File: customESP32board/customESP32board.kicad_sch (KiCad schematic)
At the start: 27 parts, among them J1 USB_B_Micro, J2 Conn_01x16_Pin, J3 Conn_01x16_Pin, Q1 S8050, Q2 S8050, SW1 SW_Push, SW2 SW_Push, U1 ESP32-WROOM-32, U2 CH340C, U3 AMS1117-3.3

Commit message: finalized esp32 board schematic
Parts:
- added D6, D7, D8: LED_BGKR, symbol Device:LED_BGKR
- added R7, R8, R9: 220 Ohm, symbol Device:R
- R1, R4: value 80 Ohm -> 1k Ohm
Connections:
- net ESP_RXD is gone; now on net ESP_U0TX: U2.3 (RXD)
- net ESP_TXD is gone; now on net ESP_U0RX: U2.2 (TXD)
- net ESP_IO0: now also U1.25 (IO0)
- net ESP_IO12: now also U1.14 (IO12)
- net ESP_IO13: now also U1.16 (IO13)
- net ESP_IO14: now also U1.13 (IO14)
- net ESP_IO15: now also U1.23 (IO15)
- net ESP_IO16: now also U1.27 (IO16)
- net ESP_IO17: now also U1.28 (IO17)
- net ESP_IO18: now also U1.30 (IO18), R9.1
- net ESP_IO19: now also U1.31 (IO19), R8.1
- net ESP_IO2: now also U1.24 (IO2)
- net ESP_IO21: now also U1.33 (IO21), R7.1
- net ESP_IO22: now also U1.36 (IO22)
- net ESP_IO23: now also U1.37 (IO23)
- net ESP_IO25: now also U1.10 (IO25)
- net ESP_IO26: now also U1.11 (IO26)
- net ESP_IO27: now also U1.12 (IO27)
- net ESP_IO32: now also U1.8 (IO32)
- net ESP_IO4: now also U1.26 (IO4)
- net ESP_IO5: now also U1.29 (IO5)
- net ESP_U0RX: now also U1.34 (RXD0/IO3)
- net ESP_U0TX: now also U1.35 (TXD0/IO1)
- net GND: now also D6.3 (K), D7.3 (K), D8.3 (K)
- new net RGB_BLUE: D6.1 (BA), D7.1 (BA), D8.1 (BA), R7.2
- new net RGB_GREEN: D6.2 (GA), D7.2 (GA), D8.2 (GA), R8.2
- new net RGB_RED: D6.4 (RA), D7.4 (RA), D8.4 (RA), R9.2
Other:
- note added: "3 RGBs common Cathode"
- note added: "BOOT"
- note added: "ESP32-Wroom-32"
- note added: "Reset"
- moved on the sheet: C1, C11, C3, C6, C7, D1, D2, D3, D4, D5, D9, J1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

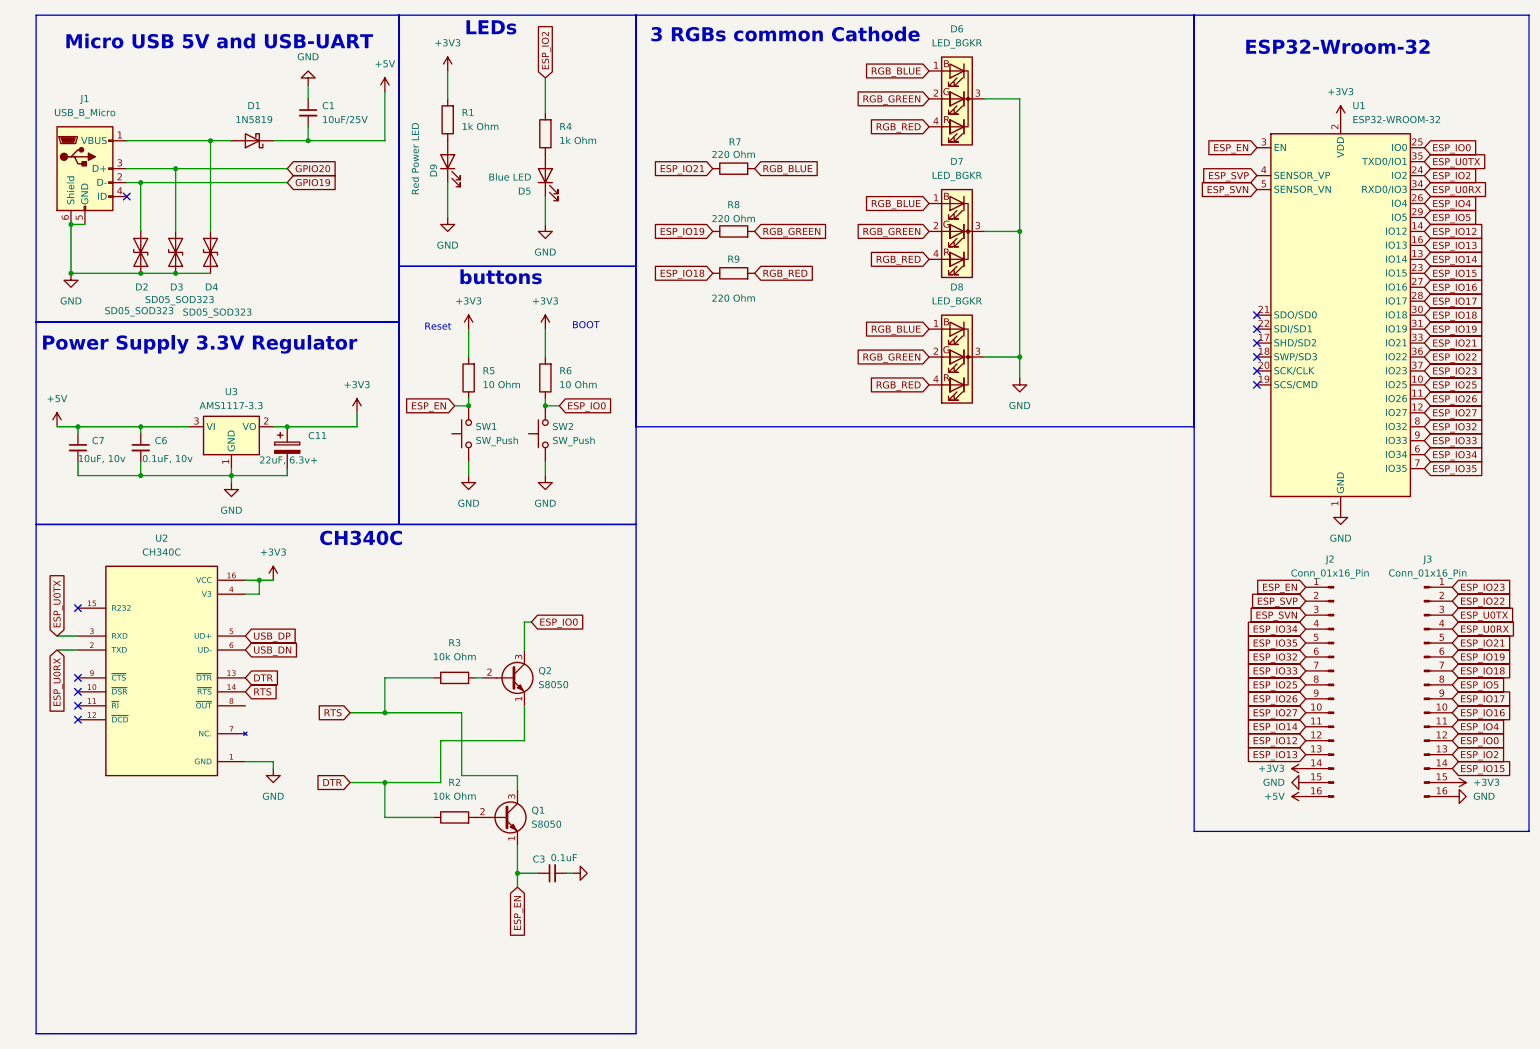
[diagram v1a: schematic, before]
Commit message: calculated LEDs current limiting resistance for power and test led D9 and D5
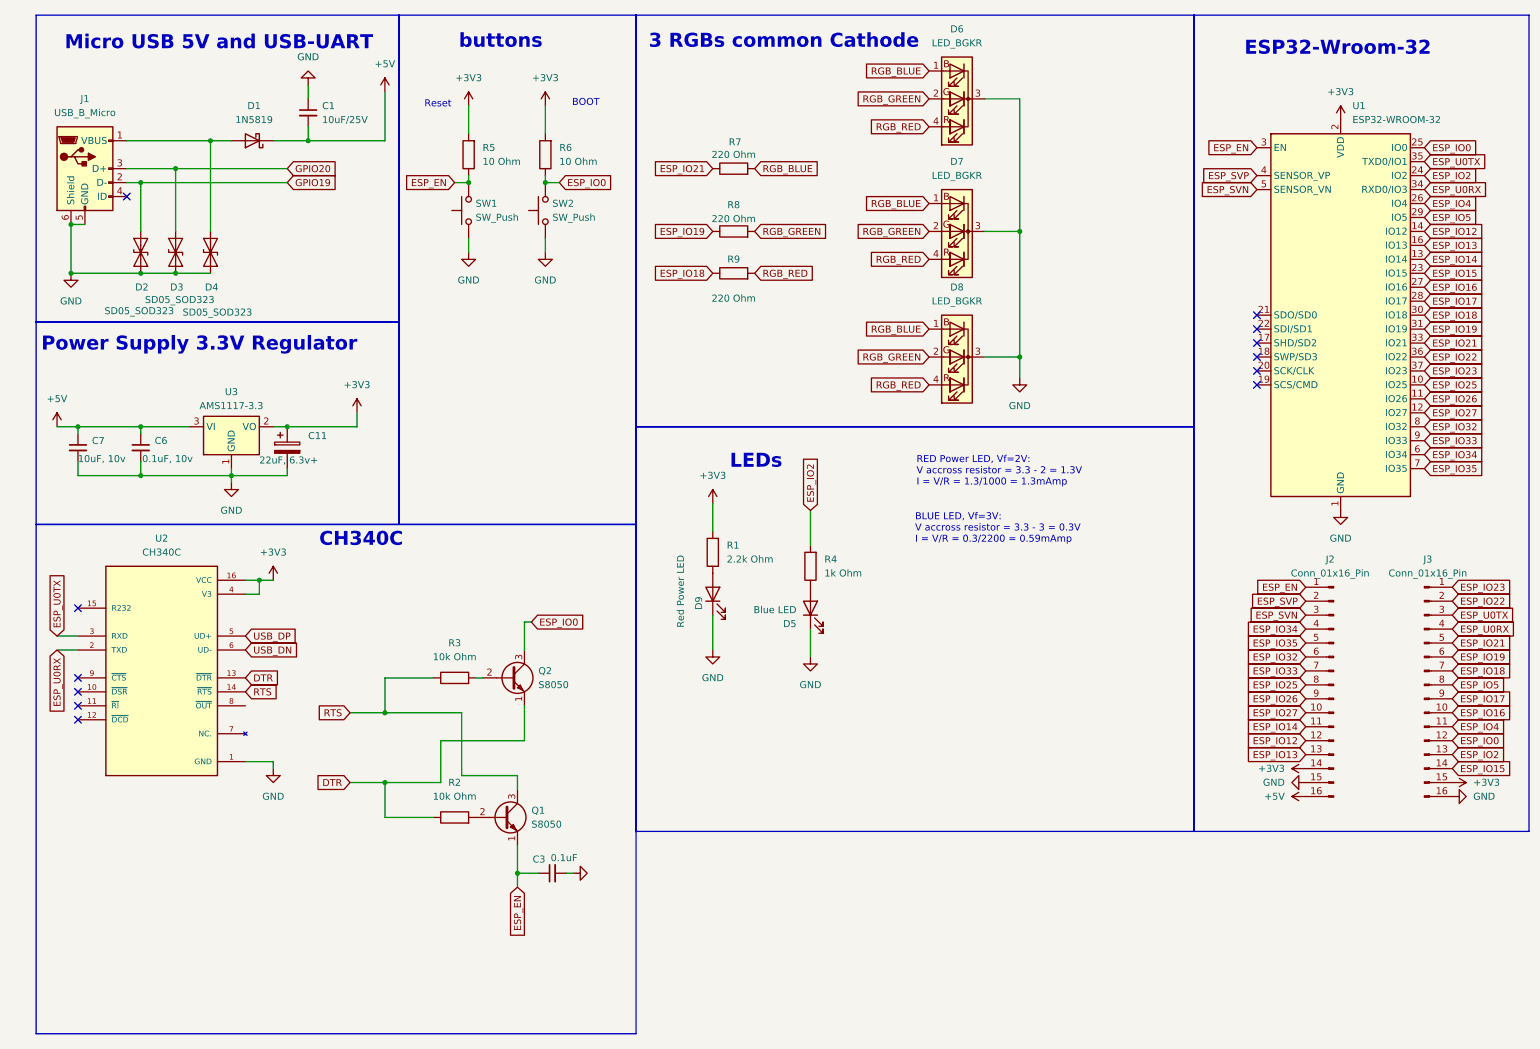
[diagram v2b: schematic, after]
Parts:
- R1: value 1k Ohm -> 2.2k Ohm
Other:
- note added: "BLUE LED, Vf=3V: V accross resistor = 3.3 - 3 = 0.3V I = V/R = 0.3/2200 = 0.59mAmp"
- note added: "RED Power LED, Vf=2V: V accross resistor = 3.3 - 2 = 1.3V I = V/R = 1.3/1000 = 1.3mAmp"
- moved on the sheet: D5, D9, R1, R4, R5, R6, SW1, SW2

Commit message: added RGB controlled by esp32 pins using N channel MOSFET bss138
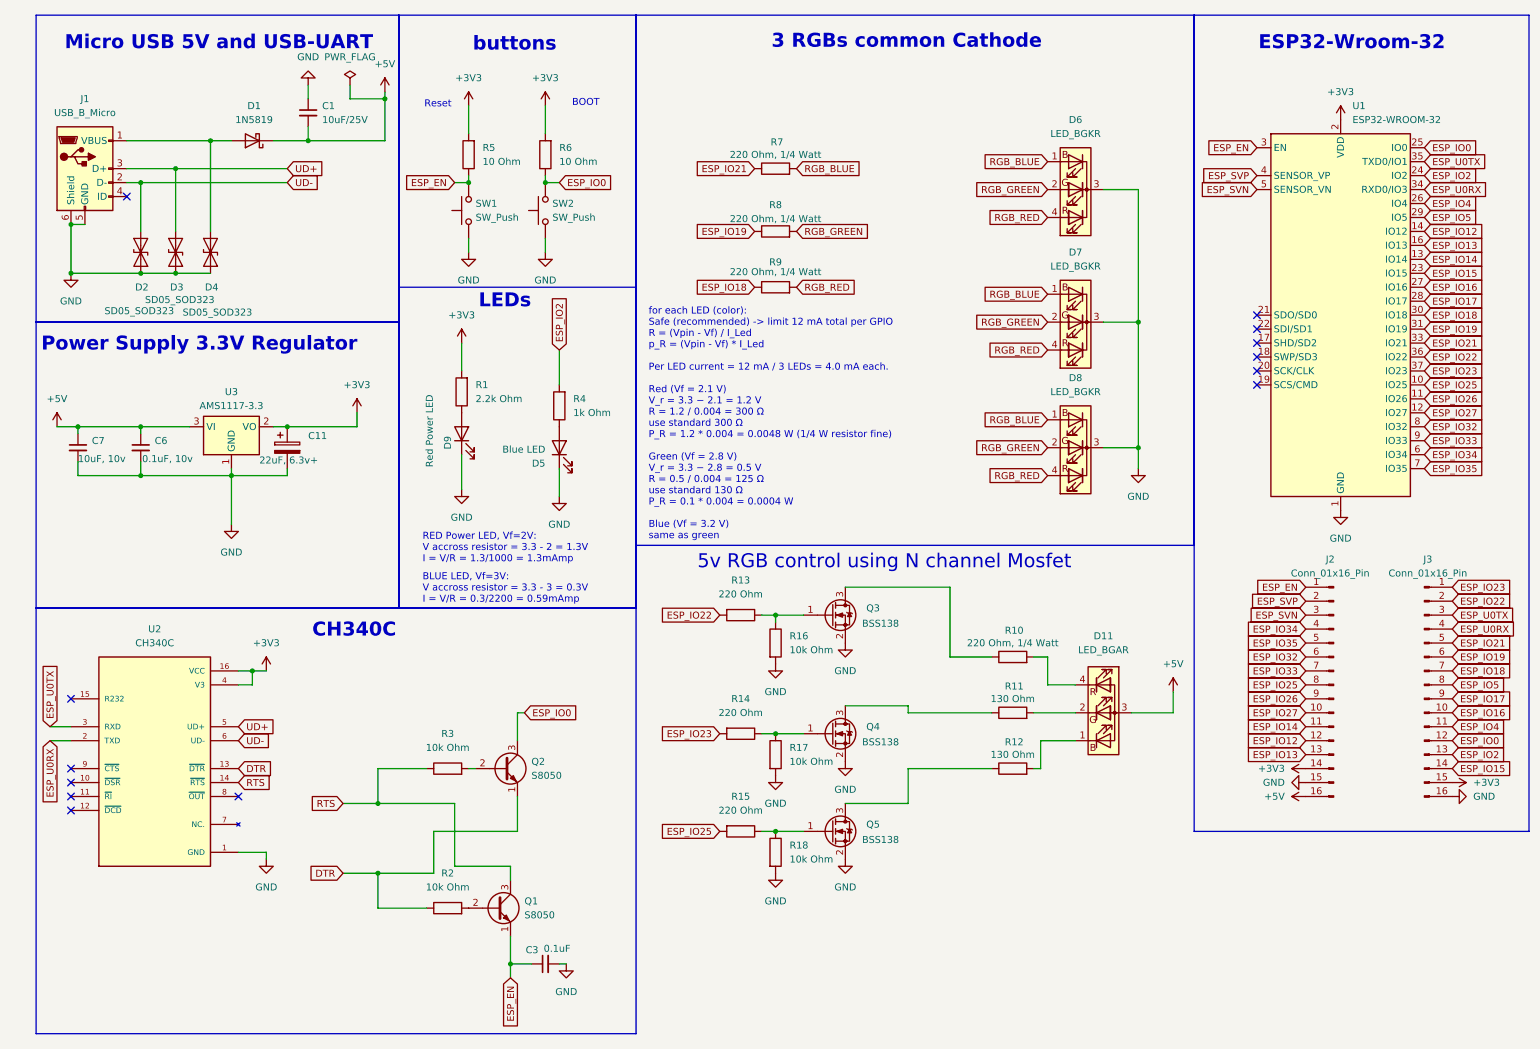
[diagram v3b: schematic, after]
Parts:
- added D11: LED_BGAR, symbol Device:LED_BGAR
- added Q3, Q4, Q5: BSS138, Package_TO_SOT_SMD:SOT-23, symbol Transistor_FET:BSS138
- added R10: 220 Ohm, 1/4 Watt, symbol Device:R
- added R11, R12: 130 Ohm, symbol Device:R
- added R13, R14, R15: 220 Ohm, symbol Device:R
- added R16, R17, R18: 10k Ohm, symbol Device:R
- D1: link (none) -> https://uge-one.com/product/smd-schottky-diode-1n5819-ss14-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
- D2, D3, D4: link (none) -> https://uge-one.com/product/smd-tvs-esd-protection-diode-bi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
- D5, D9: link (none) -> https://makerselectronics.com/product/smd-led-0603/?srsltid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
- D6, D7, D8: link (none) -> https://makerselectronics.com/product/rgb-diffused-led-comm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
- J1: link (none) -> https://uge-one.com/product/micro-usb-5pin-smd-connector-4-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
- Q1, Q2: link (none) -> https://makerselectronics.com/product/smd-transistor-s8050-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
- R1: link (none) -> https://makerselectronics.com/product/chip-resistor-smd-2-2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
- R2, R3: link (none) -> https://makerselectronics.com/product/chip-resistor-smd-10k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
- R4: link (none) -> https://makerselectronics.com/product/chip-resistor-smd-1k%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
- R5, R6: link (none) -> https://makerselectronics.com/product/chip-resistor-smd-10%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
- R7, R8, R9: value 220 Ohm -> 220 Ohm, 1/4 Watt; link (none) -> https://uge-one.com/product/smd-chip-resistor-size-0603-220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
- SW1, SW2: link (none) -> https://uge-one.com/product/smd-micro-push-button-switch-2p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
- U1: link (none) -> https://uge-one.com/product/espressif-esp32-wroom-32-dual-c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
- U2: link (none) -> https://makerselectronics.com/product/ch340c-smd-ic-transce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
- U3: link (none) -> https://makerselectronics.com/product/ams1117-3-3v-smd-fixe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
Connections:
- net USB_DN is gone; now on net UD-: U2.6 (UD-)
- net USB_DP is gone; now on net UD+: U2.5 (UD+)
- net +5V: now also D11.3 (A)
- net ESP_IO22: now also R13.2
- net ESP_IO23: now also R14.2
- net ESP_IO25: now also R15.2
- net GND: now also Q3.2 (S), Q4.2 (S), Q5.2 (S), R16.2, R17.2, R18.2
- net GPIO19 renamed UD-
- net GPIO20 renamed UD+
- new net: Q3.1 (G), R13.1, R16.1
- new net: Q4.3 (D), R11.1
- new net: D11.2 (GK), R11.2
- new net: Q5.3 (D), R12.1
- new net: D11.1 (BK), R12.2
- new net: Q5.1 (G), R15.1, R18.1
- new net: Q3.3 (D), R10.1
- new net: D11.4 (RK), R10.2
- new net: Q4.1 (G), R14.1, R17.1
- no-connect marks 12 -> 13
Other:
- note added: "5v RGB control using N channel Mosfet"
- note added: "for each LED (color): Safe (recommended) -> limit 12 mA total per GPIO R = (Vpin - Vf) / I_Led p_R = (Vpin - Vf) * I_Led Per LED current = 12 mA / 3 LEDs = 4.0 mA each. Red (Vf = 2.1 V) V_r = 3.3 − 2.1 = 1.2 V R = 1.2 / 0.004 = 300 Ω use standard 300 Ω P_R = 1.2 * 0.004 = 0.0048 W (1/4 W resistor fine) Green (Vf = 2.8 V) V_r = 3.3 − 2.8 = 0.5 V R = 0.5 / 0.004 = 125 Ω use standard 130 Ω P_R = 0.1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"
- moved on the sheet: C3, D5, D6, D7, D8, D9, Q1, Q2, R1, R2, R3, R4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

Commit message: assigned CH340C footprint library
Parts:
- U2: footprint CH340C:SOIC127P600X180-16N -> CH340C:CH340C
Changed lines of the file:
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@@
 			)
 		)
-		(property "Footprint" "CH340C:SOIC127P600X180-16N"
+		(property "Footprint" "CH340C:CH340C"
 			(at 34.29 149.86 0)
 			(effects
